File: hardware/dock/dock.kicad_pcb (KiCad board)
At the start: 2 copper layers, 100 x 100 mm, 69 parts, among them J1 L-KLS1-5416-L1-01-R, J2 Conn_01x05_Pin, J3 Conn_01x05_Pin, J4 L-KLS1-5416-L1-01-R, J5 L-KLS1-5416-L1-01-R, J6 Conn_01x05_Pin, J7 Conn_01x06, J8 Conn_01x05_Pin, U1 TPS2116DRL, U3 TPS2553DBVR, U4 TPD4E1U06DBVR, U5 TPD4E1U06DBVR, U6 TPD4E1U06DBVR, U7 XIAO_nRF52840, U8 TPS2552DBVR, U9 TPD4E1U06DBVR

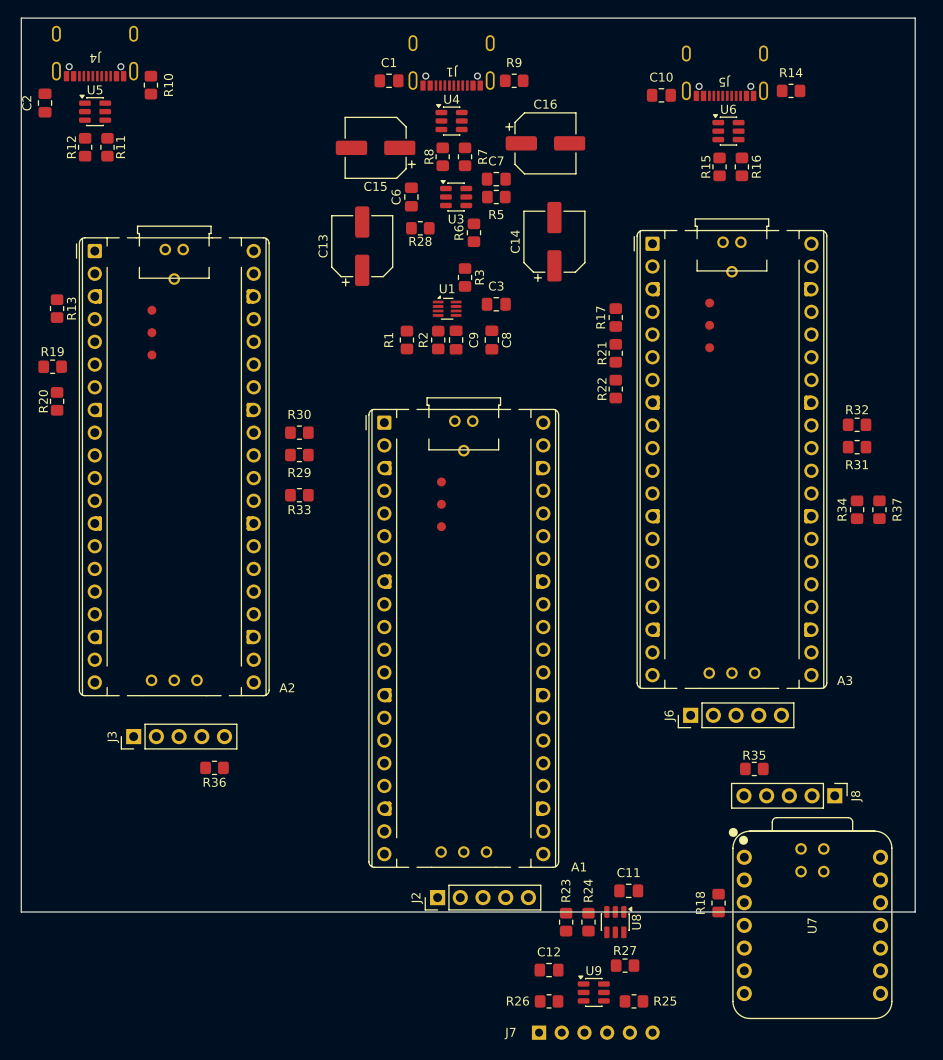
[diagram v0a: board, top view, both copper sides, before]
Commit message: Host becomes Pico 2 W (on-board BLE); remove XIAO nRF52840
- A1 -> Raspberry Pi Pico 2 W, new footprint RaspberryPi_Pico2W_Socket_Pogo
  (TP1-3 probes unchanged, SWD via 1x3 socket under the debug holes,
  TP4-6 at Pico 2 W positions, 14x9 mm antenna keep-out)
- Remove U7 (XIAO), J8 and R35; BLE UART and BLE_RST_CTRL gone
- Pogo TX/RX/DET now go to the host: GP16 (PIO TX), GP17 (PIO RX),
  GP22 (DET); R18 pulls DET up to HOST_3V3
- HID-A: CC1/CC2 on U5 and R29/R30 swapped for routing (user change)
- DESIGN.md/README/PCB_PLACEMENT.md updated; board includes in-progress
  routing and B.Cu GND zone (not yet updated from schematic)

Co-Authored-By: Claude Opus 5.5 <noreply@anthropic.com>
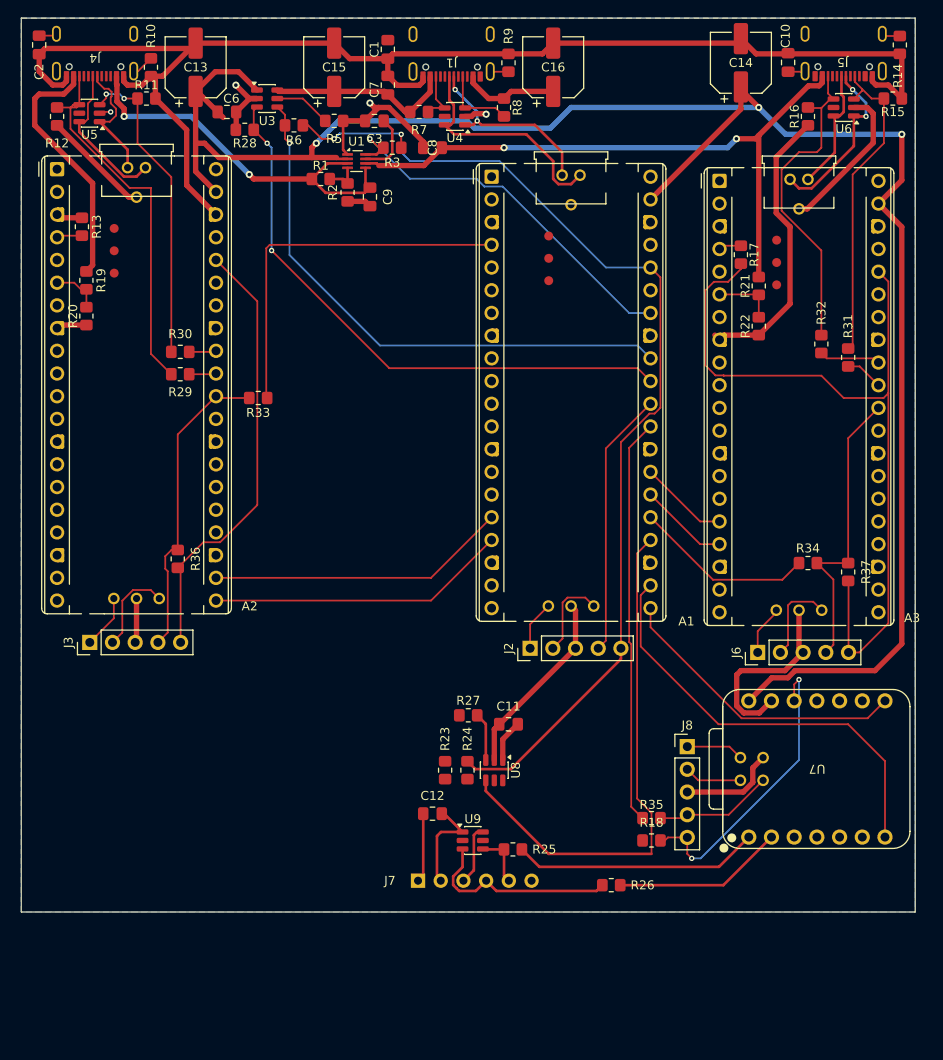
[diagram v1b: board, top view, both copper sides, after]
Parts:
- moved R27 33.0 mm to (110.5, 103.5)
- moved A1 30.0 mm to (113.1, 43.2)
- moved J2 29.7 mm to (117.4, 96.0)
- moved C14 28.9 mm to (141.0, 30.5)
- moved C13 27.3 mm to (80.0, 31.0)
- moved C3 24.6 mm to (100.0, 37.0), turned to 0 degrees
- moved U3 23.8 mm to (88.0, 34.5)
- moved R36 23.7 mm to (78.0, 86.0), turned to 90 degrees
- moved R6 23.4 mm to (91.0, 37.5), turned to 180 degrees
- moved C11 23.0 mm to (115.0, 104.5)
- moved C6 22.7 mm to (83.5, 36.0), turned to 180 degrees
- moved R28 22.5 mm to (85.5, 38.0)
- moved C8 22.5 mm to (106.5, 40.0), turned to 180 degrees
- moved C12 21.8 mm to (106.5, 114.5)
- moved R23 21.7 mm to (107.9, 109.6)
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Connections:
- A1 pad 1: HID_PERSONAL_TX -> unconnected-(A1-GPIO0-Pad1)
- A1 pad 11: BLE_UART_TX -> unconnected-(A1-GPIO8-Pad11)
- A1 pad 12: BLE_UART_RX -> unconnected-(A1-GPIO9-Pad12)
- A1 pad 16: unconnected-(A1-GPIO12-Pad16) -> HID_PERSONAL_TX
- A1 pad 17: unconnected-(A1-GPIO13-Pad17) -> HID_PERSONAL_RX
- A1 pad 2: HID_PERSONAL_RX -> unconnected-(A1-GPIO1-Pad2)
- A1 pad 21: KEYBOARD_VBUS_EN -> BLE_UART_TX
- A1 pad 22: KEYBOARD_VBUS_FAULT -> BLE_UART_RX
- A1 pad 24: MUX_STATUS -> POGO_5V_FAULT
- A1 pad 25: HID_PERSONAL_RUN_CTRL -> HID_WORK_RUN_CTRL
- A1 pad 26: POGO_5V_FAULT -> HID_WORK_TX
- A1 pad 27: HID_WORK_RUN_CTRL -> HID_WORK_RX
- A1 pad 31: unconnected-(A1-GPIO26_ADC0-Pad31) -> KEYBOARD_VBUS_EN
- A1 pad 32: unconnected-(A1-GPIO27_ADC1-Pad32) -> KEYBOARD_VBUS_FAULT
- A1 pad 34: unconnected-(A1-GPIO28_ADC2-Pad34) -> MUX_STATUS
- A1 pad 4: unconnected-(A1-GPIO2-Pad4) -> HID_PERSONAL_RUN_CTRL
- A1 pad 6: HID_WORK_TX -> unconnected-(A1-GPIO4-Pad6)
- A1 pad 7: HID_WORK_RX -> unconnected-(A1-GPIO5-Pad7)
- A2 pad 1: HID_PERSONAL_RX -> unconnected-(A2-GPIO0-Pad1)
- A2 pad 2: HID_PERSONAL_TX -> unconnected-(A2-GPIO1-Pad2)
- A2 pad 21: unconnected-(A2-GPIO16-Pad21) -> HID_PERSONAL_RX
- A2 pad 22: unconnected-(A2-GPIO17-Pad22) -> HID_PERSONAL_TX
- A3 pad 1: HID_WORK_RX -> unconnected-(A3-GPIO0-Pad1)
- A3 pad 16: unconnected-(A3-GPIO12-Pad16) -> HID_WORK_RX
- A3 pad 17: unconnected-(A3-GPIO13-Pad17) -> HID_WORK_TX
- A3 pad 2: HID_WORK_TX -> unconnected-(A3-GPIO1-Pad2)
- R29 pad 2: /HID_PERSONAL/CC1 -> /HID_PERSONAL/CC2
- R30 pad 2: /HID_PERSONAL/CC2 -> /HID_PERSONAL/CC1
- U5 pad 3: /HID_PERSONAL/CC2 -> /HID_PERSONAL/CC1
- U5 pad 4: /HID_PERSONAL/CC1 -> /HID_PERSONAL/CC2
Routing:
- net GND: track 0.00 -> 319.6 mm, vias 0 -> 4
- net SYS_5V: track 0.00 -> 224.4 mm, vias 0 -> 3
- net HOST_3V3: track 0.00 -> 117.8 mm, vias 0 -> 2
- net /HID_WORK/PICO_3V3: track 0.00 -> 89.8 mm
- net WORK_VBUS: track 0.00 -> 71.6 mm, vias 0 -> 2
- net PERSONAL_VBUS: track 0.00 -> 71.5 mm, vias 0 -> 2
- net KEYBOARD_VBUS_EN: track 0.00 -> 65.5 mm, vias 0 -> 2
- net KEYBOARD_VBUS_FAULT: track 0.00 -> 62.3 mm, vias 0 -> 1
- net POGO_5V_FAULT: track 0.00 -> 59.0 mm
- net /HID_PERSONAL/PICO_3V3: track 0.00 -> 49.9 mm
- net BLE_UART_RX: track 0.00 -> 48.4 mm
- net BLE_RST_CTRL: track 0.00 -> 45.4 mm
- net MUX_STATUS: track 0.00 -> 43.7 mm, vias 0 -> 1
- net /HID_PERSONAL/CC2: track 0.00 -> 42.5 mm
- net HID_PERSONAL_RUN_CTRL: track 0.00 -> 42.2 mm
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- added copper zone on B.Cu, net GND

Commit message: Dock PCB routing complete; add dock BOM
- Board: all nets routed, 0 unconnected, 0 schematic-parity errors;
  B.Cu GND plane; USB-C second D+/D-/VBUS pads and shield tabs joined;
  power paths at 0.6 mm with short neck-downs at U1
- Remaining DRC: courtyard overlaps for resistors under the Picos
  (excluded, intentional) and minor silkscreen notes
- hardware/dock/BOM.xlsx: 28 lines (66 schematic parts + mechanical +
  PCB) with editable spares/pack/price/shop/URL and formula totals

Co-Authored-By: Claude Opus 5.5 <noreply@anthropic.com>
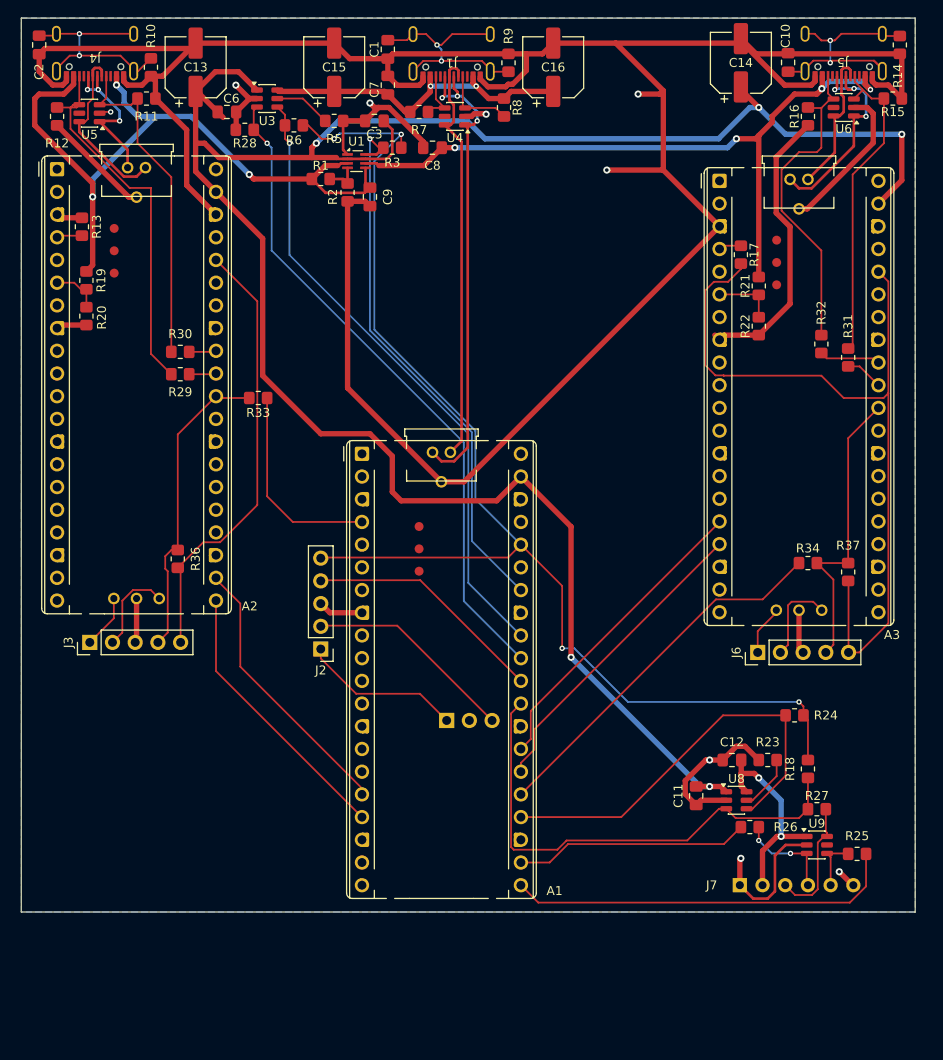
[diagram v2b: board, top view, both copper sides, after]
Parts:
- removed J8: Conn_01x05_Pin, Connector_PinHeader_2.54mm:PinHeader_1x05_P2.54mm_Vertical
- removed R35: 1k, Resistor_SMD:R_0805_2012Metric_Pad1.20x1.40mm_HandSolder
- removed U7: XIAO_nRF52840, dock:XIAO_nRF52840_Socket_Pogo
- A1: value Raspberry Pi Pico 2 -> Raspberry Pi Pico 2 W; footprint dock:RaspberryPi_Pico2_Socket_Pogo -> dock:RaspberryPi_Pico2W_Socket_Pogo
- moved R27 40.4 mm to (149.5, 114.0), turned to 180 degrees
- moved R25 38.5 mm to (154.0, 119.0)
- moved U9 38.5 mm to (149.5, 118.0)
- moved R24 37.1 mm to (147.0, 103.5), turned to 180 degrees
- moved R23 36.1 mm to (144.0, 108.5), turned to 180 degrees
- moved J7 36.0 mm to (147.2, 122.5)
- moved A1 34.2 mm to (98.6, 74.2)
- moved C12 34.0 mm to (140.0, 108.5)
- moved U8 27.3 mm to (140.5, 113.0), turned to 0 degrees
- moved J2 23.4 mm to (94.0, 96.1), turned to 180 degrees
- moved C11 22.5 mm to (136.0, 112.5), turned to -90 degrees
- moved R18 19.2 mm to (148.5, 109.5), turned to 90 degrees
- moved R26 16.8 mm to (142.0, 116.0), turned to 180 degrees
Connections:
- A1 pad 21: BLE_UART_TX -> POGO_TX
- A1 pad 22: BLE_UART_RX -> POGO_RX
- A1 pad 29: BLE_RST_CTRL -> POGO_DET
- R18 pad 1: /BLE_BASE/POGO_DET -> POGO_DET
- R18 pad 2: /BLE_BASE/XIAO_3V3 -> HOST_3V3
- R25 pad 2: /BLE_BASE/POGO_TX -> POGO_TX
- R26 pad 2: /BLE_BASE/POGO_RX -> POGO_RX
- R27 pad 2: /BLE_BASE/POGO_DET -> POGO_DET
- U8 pad 3: /BLE_BASE/POGO_DET -> POGO_DET
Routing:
- net GND: track 319.6 -> 436.4 mm, vias 4 -> 9
- net POGO_DET: track 0.00 -> 56.1 mm
- net BLE_UART_RX: track 48.4 -> 0.00 mm
- net BLE_RST_CTRL: track 45.4 -> 0.00 mm
- net POGO_TX: track 0.00 -> 43.8 mm
- net /BLE_BASE/XIAO_3V3: track 33.8 -> 0.00 mm, vias 2 -> 0
- net BLE_UART_TX: track 33.4 -> 0.00 mm
- net USB_HOST_D_P: track 21.1 -> 53.4 mm, vias 2 -> 3
- net /BLE_BASE/POGO_TX: track 27.6 -> 0.00 mm
- net POGO_RX: track 0.00 -> 26.3 mm
- net Net-(J1-SHIELD): track 2.05 -> 28.0 mm, vias 0 -> 2
- net HID_WORK_TX: track 10.0 -> 34.7 mm
- net HID_WORK_RX: track 10.0 -> 34.7 mm
- net Net-(J5-SHIELD): track 3.99 -> 26.4 mm, vias 0 -> 2
- net HOST_3V3: track 117.8 -> 139.8 mm, vias 2 -> 4
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
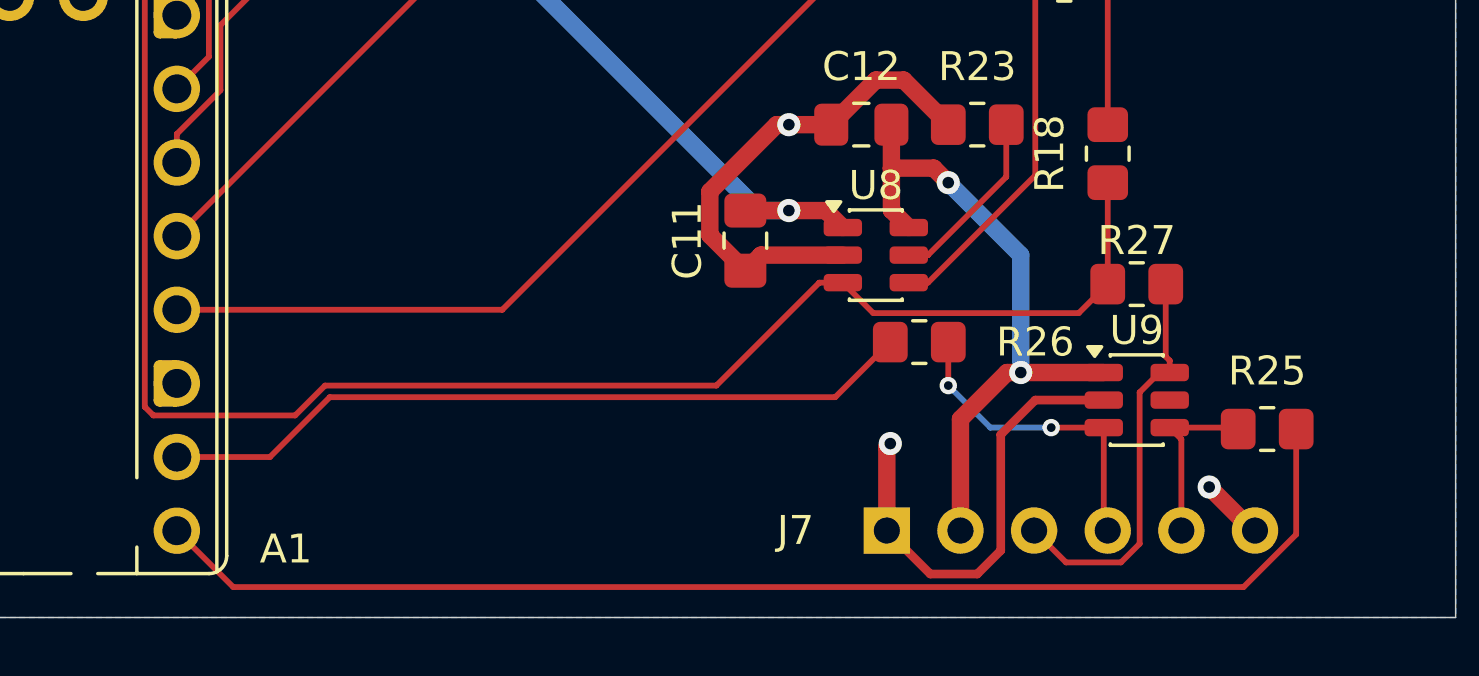
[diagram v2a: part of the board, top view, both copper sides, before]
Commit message: Dock PCB: J7 moved to board edge, zones refilled; add JLCPCB fab outputs
Co-Authored-By: Claude Opus 5.5 <noreply@anthropic.com>
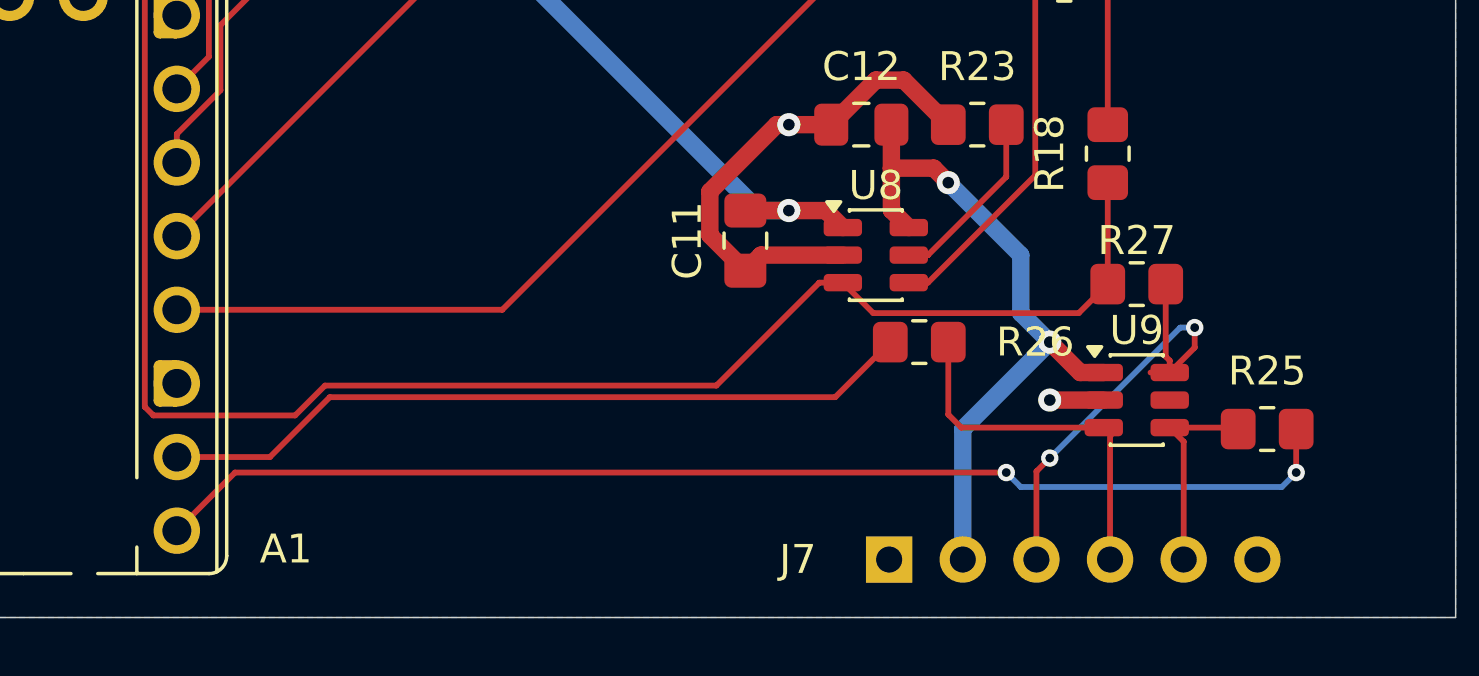
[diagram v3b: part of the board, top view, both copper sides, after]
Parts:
- moved J7 1.00 mm to (147.3, 123.5)
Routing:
- net GND: track 436.4 -> 420.1 mm, vias 9 -> 8
- net POGO_TX: track 43.8 -> 41.4 mm, vias 0 -> 2
- net /BLE_BASE/POGO_DET_CONN: track 14.0 -> 16.2 mm, vias 0 -> 2
- net /BLE_BASE/POGO_RX_CONN: track 11.1 -> 13.1 mm, vias 2 -> 0
- net /BLE_BASE/POGO_TX_CONN: track 6.10 -> 7.13 mm
- net /BLE_BASE/POGO_5V: track 23.0 -> 24.0 mm

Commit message: Dock: add six M3 mounting holes; BOM gets PCB price, USD rate cell and 1x19 socket note
Co-Authored-By: Claude Opus 5.5 <noreply@anthropic.com>
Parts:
- added H1: MountingHole_3.2mm_M3, MountingHole:MountingHole_3.2mm_M3, F.Cu at (93.2, 47.5)
- added H2: MountingHole_3.2mm_M3, MountingHole:MountingHole_3.2mm_M3, F.Cu at (126.2, 34.9)
- added H3: MountingHole_3.2mm_M3, MountingHole:MountingHole_3.2mm_M3, F.Cu at (64.5, 121.5)
- added H4: MountingHole_3.2mm_M3, MountingHole:MountingHole_3.2mm_M3, F.Cu at (157.5, 106.0)
- added H5: MountingHole_3.2mm_M3, MountingHole:MountingHole_3.2mm_M3, F.Cu at (126.7, 108.9)
- added H6: MountingHole_3.2mm_M3, MountingHole:MountingHole_3.2mm_M3, F.Cu at (64.0, 99.0)
